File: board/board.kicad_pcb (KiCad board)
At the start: 2 copper layers, 43.2 x 53.3 mm, 73 parts, among them U2 10M02SCE144

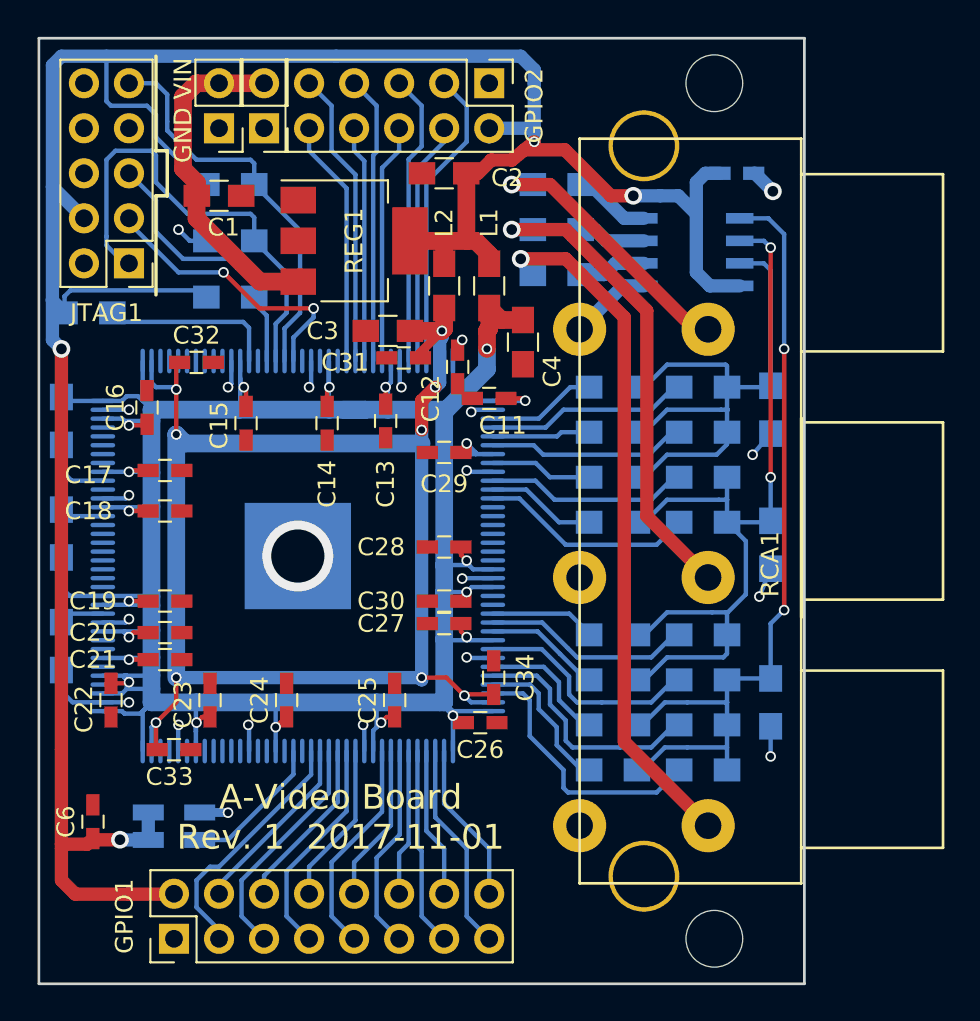
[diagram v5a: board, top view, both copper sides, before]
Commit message: Complete redo of the board
In Rev.1 I got GND and Line mixed up for the Video line sockets. As I
had to modify the board anyway, I also changed the location of the FPGA
from backside to front side and therefore had to redo everything.
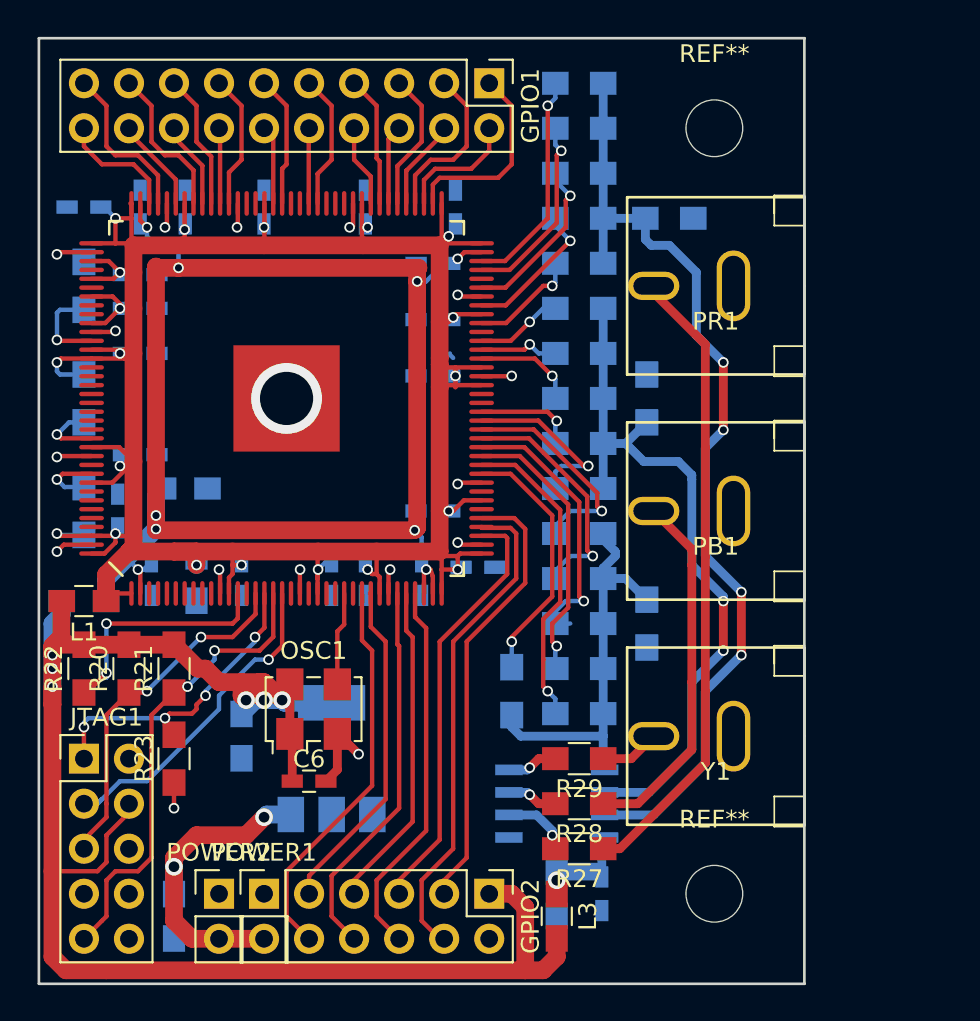
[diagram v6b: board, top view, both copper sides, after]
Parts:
- removed ? (x2): MountingHole_3.2mm_M3, Mounting_Holes:MountingHole_3.2mm_M3
- removed ?: CONN_02X01, Pin_Headers:Pin_Header_Straight_1x02_Pitch2.54mm
- removed C28, C29, C30: 100nF, Capacitors_SMD:C_0603_HandSoldering
- removed GND VIN: CONM_01x02, Pin_Headers:Pin_Header_Straight_1x02_Pitch2.54mm
- removed RCA1: TrippleRCA, footprints:TrippleRCA
- added C5: 10uF, Capacitors_SMD:C_0805_HandSoldering, B.Cu at (146.1, 119.4)
- added L3: 10mH, Capacitors_SMD:C_0805_HandSoldering, F.Cu at (146.1, 120.7)
- added PB1: BNC, footprints:RCA_JACK, F.Cu at (160.0, 97.8)
- added POWER1: CONM_01x02, Pin_Headers:Pin_Header_Straight_1x02_Pitch2.54mm, F.Cu at (129.5, 119.4)
- added POWER2: CONN_02X01, Pin_Headers:Pin_Header_Straight_1x02_Pitch2.54mm, F.Cu at (127.0, 119.4)
- added PR1: BNC, footprints:RCA_JACK, F.Cu at (160.0, 85.1)
- added REF**: MountingHole_3.2mm_M3, Mounting_Holes:MountingHole_3.2mm_M3, F.Cu at (154.9, 119.4)
- added REF**: MountingHole_3.2mm_M3, Mounting_Holes:MountingHole_3.2mm_M3, F.Cu at (154.9, 76.2)
- added Y1: BNC, footprints:RCA_JACK, F.Cu at (160.0, 110.5)
- C1, C11, C12, C13, C14, C15, C16, C17, C18, C19, C2, C20, C21, C22, C23, C24, C25, C26, C27, C3, C31, C32, C33, C34, C4, L2, REG1: moved to B.Cu
- GPIO1: value CONN_02X08 -> CONN_02X10; footprint Pin_Headers:Pin_Header_Straight_2x08_Pitch2.54mm -> Pin_Headers:Pin_Header_Straight_2x10_Pitch2.54mm
- OSC1: value XO32050UITA -> LFSPXO024957; footprint Oscillators:Oscillator_SMD_EuroQuartz_XO32-4pin_3.2x2.5mm_HandSoldering -> Oscillators:Oscillator_SMD_EuroQuartz_XO53-4pin_5.0x3.2mm_HandSoldering; moved to F.Cu
- R1: value 1k -> 1k1
- R10: value 10k -> 8k
- R11: value 10k -> 16k
- R14, R9: value 10k -> 4k
- R15: value 4k -> 8k
- R16: value 8k -> 16k
- R17: value 16k -> 150
- R19: value 1k -> 150
- R2: value 150 -> 1k
- R20: value 2k -> 10k; moved to F.Cu
- R21: value 4k -> 10k; moved to F.Cu
- R22: value 8k -> 10k; moved to F.Cu
- R23: value 16k -> 10k; moved to F.Cu
- R27, R28, R29, U2: moved to F.Cu
- R7: value 1k1 -> 1k
- R8: value 150 -> 2k
- moved GPIO1 51.4 mm to (142.2, 73.7), turned to 270 degrees
- moved GPIO2 45.7 mm to (142.2, 119.4)
- moved C7 41.3 mm to (148.6, 119.4), turned to 90 degrees
- moved C1 40.7 mm to (124.5, 120.7), turned to 270 degrees
- moved R27 37.5 mm to (147.3, 116.8), turned to 180 degrees
- moved C2 33.7 mm to (128.3, 110.5), turned to 270 degrees
- moved R28 32.4 mm to (147.3, 114.3), turned to 180 degrees
- moved AMP1 32.0 mm to (146.1, 114.3)
- moved R16 31.9 mm to (147.3, 73.7)
- moved R22 30.4 mm to (119.4, 106.7), turned to 90 degrees
- moved R21 30.0 mm to (124.5, 106.7), turned to 90 degrees
- moved R23 29.9 mm to (124.5, 111.8), turned to 90 degrees
- moved REG1 29.2 mm to (133.3, 111.8), turned to 90 degrees
- moved L1 29.0 mm to (119.4, 102.9), turned to 180 degrees
- moved R15 28.6 mm to (147.3, 76.2)
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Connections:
- AMP1 pad 4: /3V3A -> /3V3D
- C7 pad 2: /3V3A -> /3V3D
- GPIO1 pad 1: GND -> Net-(GPIO1-Pad1)
- GPIO1 pad 2: /3V3A -> Net-(GPIO1-Pad2)
- GPIO2 pad 1: GND -> /3V3A
- GPIO2 pad 2: /3V3A -> GND
- R1 pad 2: Net-(AMP1-Pad3) -> Net-(AMP1-Pad1)
- R10 pad 1: Net-(JTAG1-Pad9) -> Net-(R10-Pad1)
- R10 pad 2: /3V3A -> Net-(AMP1-Pad2)
- R11 pad 2: /3V3A -> Net-(AMP1-Pad2)
- R12 pad 2: Net-(AMP1-Pad2) -> Net-(AMP1-Pad3)
- R13 pad 2: Net-(AMP1-Pad2) -> Net-(AMP1-Pad3)
- R14 pad 1: GND -> Net-(R14-Pad1)
- R14 pad 2: Net-(JTAG1-Pad1) -> Net-(AMP1-Pad3)
- R15 pad 2: Net-(AMP1-Pad2) -> Net-(AMP1-Pad3)
- R16 pad 2: Net-(AMP1-Pad2) -> Net-(AMP1-Pad3)
- R17 pad 1: Net-(R17-Pad1) -> Net-(AMP1-Pad1)
- R17 pad 2: Net-(AMP1-Pad2) -> GND
- R18 pad 1: Net-(AMP1-Pad1) -> Net-(AMP1-Pad2)
- R19 pad 1: Net-(R19-Pad1) -> Net-(AMP1-Pad3)
- R19 pad 2: Net-(AMP1-Pad1) -> GND
- R2 pad 1: Net-(AMP1-Pad3) -> Net-(R2-Pad1)
- R2 pad 2: GND -> Net-(AMP1-Pad1)
- R20 pad 1: Net-(R20-Pad1) -> Net-(JTAG1-Pad5)
- R20 pad 2: Net-(AMP1-Pad1) -> /3V3A
- R21 pad 1: Net-(R21-Pad1) -> Net-(JTAG1-Pad9)
- R21 pad 2: Net-(AMP1-Pad1) -> /3V3A
- R22 pad 2: Net-(AMP1-Pad1) -> /3V3A
- R23 pad 1: Net-(R23-Pad1) -> GND
- R23 pad 2: Net-(AMP1-Pad1) -> Net-(JTAG1-Pad1)
- R27 pad 2: Net-(AMP1-Pad8) -> Net-(AMP1-Pad6)
- R29 pad 2: Net-(AMP1-Pad6) -> Net-(AMP1-Pad8)
- R3 pad 2: Net-(AMP1-Pad3) -> Net-(AMP1-Pad1)
- R4 pad 2: Net-(AMP1-Pad3) -> Net-(AMP1-Pad1)
- R5 pad 2: Net-(AMP1-Pad3) -> Net-(AMP1-Pad1)
- R6 pad 2: Net-(AMP1-Pad3) -> Net-(AMP1-Pad1)
- R8 pad 1: Net-(AMP1-Pad2) -> Net-(R8-Pad1)
- R8 pad 2: GND -> Net-(AMP1-Pad2)
- R9 pad 1: Net-(JTAG1-Pad5) -> Net-(R9-Pad1)
- R9 pad 2: /3V3A -> Net-(AMP1-Pad2)
- U2 pad 100: (no net) -> Net-(GPIO1-Pad16)
- U2 pad 101: (no net) -> Net-(GPIO1-Pad17)
- U2 pad 103: (no net) -> Net-(GPIO1-Pad18)
- U2 pad 105: (no net) -> Net-(GPIO1-Pad19)
- U2 pad 106: (no net) -> Net-(GPIO1-Pad20)
- U2 pad 13: Net-(R11-Pad1) -> Net-(R22-Pad1)
- U2 pad 24: Net-(GPIO2-Pad10) -> (no net)
- U2 pad 25: Net-(GPIO2-Pad9) -> Net-(OSC1-Pad3)
- U2 pad 26: Net-(GPIO2-Pad8) -> (no net)
- U2 pad 27: Net-(GPIO2-Pad7) -> Net-(GPIO2-Pad10)
- U2 pad 28: Net-(GPIO2-Pad6) -> Net-(GPIO2-Pad9)
- U2 pad 31: Net-(GPIO2-Pad5) -> Net-(GPIO2-Pad8)
- U2 pad 32: Net-(GPIO2-Pad4) -> Net-(GPIO2-Pad7)
- U2 pad 33: Net-(GPIO2-Pad3) -> Net-(GPIO2-Pad6)
- U2 pad 39: Net-(R1-Pad1) -> Net-(GPIO2-Pad5)
- U2 pad 40: Net-(R3-Pad1) -> Net-(GPIO2-Pad4)
- U2 pad 41: Net-(R4-Pad1) -> Net-(GPIO2-Pad3)
- U2 pad 42: Net-(R5-Pad1) -> (no net)
- U2 pad 44: Net-(R6-Pad1) -> (no net)
- U2 pad 46: Net-(R7-Pad1) -> Net-(R1-Pad1)
- U2 pad 47: Net-(R12-Pad1) -> Net-(R2-Pad1)
- U2 pad 48: Net-(R13-Pad1) -> Net-(R3-Pad1)
- U2 pad 49: (no net) -> Net-(R4-Pad1)
- U2 pad 50: (no net) -> Net-(R5-Pad1)
- U2 pad 51: (no net) -> Net-(R6-Pad1)
- U2 pad 52: (no net) -> Net-(R7-Pad1)
- U2 pad 53: (no net) -> Net-(R8-Pad1)
- U2 pad 59: (no net) -> Net-(R9-Pad1)
- U2 pad 60: (no net) -> Net-(R10-Pad1)
- U2 pad 61: Net-(R15-Pad1) -> Net-(R11-Pad1)
- U2 pad 62: Net-(R16-Pad1) -> (no net)
- U2 pad 63: Net-(R17-Pad1) -> Net-(R12-Pad1)
- U2 pad 65: Net-(R19-Pad1) -> Net-(R13-Pad1)
- U2 pad 67: Net-(R20-Pad1) -> Net-(R14-Pad1)
- U2 pad 68: Net-(R21-Pad1) -> (no net)
- U2 pad 69: Net-(R22-Pad1) -> Net-(R15-Pad1)
- U2 pad 70: Net-(R23-Pad1) -> Net-(R16-Pad1)
- U2 pad 74: Net-(GPIO1-Pad16) -> Net-(GPIO1-Pad1)
- U2 pad 75: Net-(GPIO1-Pad15) -> Net-(GPIO1-Pad2)
- U2 pad 76: Net-(GPIO1-Pad14) -> Net-(GPIO1-Pad3)
- U2 pad 77: Net-(GPIO1-Pad13) -> Net-(GPIO1-Pad4)
- U2 pad 78: Net-(GPIO1-Pad12) -> Net-(GPIO1-Pad5)
- U2 pad 79: Net-(GPIO1-Pad11) -> Net-(GPIO1-Pad6)
- U2 pad 80: Net-(GPIO1-Pad10) -> Net-(GPIO1-Pad7)
- U2 pad 81: Net-(GPIO1-Pad9) -> Net-(GPIO1-Pad8)
- U2 pad 84: Net-(GPIO1-Pad8) -> (no net)
- U2 pad 85: Net-(GPIO1-Pad7) -> (no net)
- U2 pad 86: Net-(GPIO1-Pad6) -> (no net)
- U2 pad 87: Net-(GPIO1-Pad5) -> Net-(GPIO1-Pad9)
- U2 pad 88: Net-(GPIO1-Pad4) -> Net-(GPIO1-Pad10)
- U2 pad 89: Net-(GPIO1-Pad3) -> (no net)
- U2 pad 91: Net-(OSC1-Pad3) -> Net-(GPIO1-Pad11)
- U2 pad 92: (no net) -> Net-(GPIO1-Pad12)
- U2 pad 97: (no net) -> Net-(GPIO1-Pad13)
- U2 pad 98: (no net) -> Net-(GPIO1-Pad14)
- U2 pad 99: (no net) -> Net-(GPIO1-Pad15)
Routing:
- net /3V3A: track 153.7 -> 99.8 mm, vias 4 -> 6
- net Net-(R29-Pad1): track 39.0 -> 3.38 mm, vias 1 -> 0
- net /3V3B: track 190.5 -> 166.0 mm, vias 21 -> 20
- net Net-(AMP1-Pad1): track 47.3 -> 23.2 mm, vias 2 -> 0
- net Net-(AMP1-Pad3): track 32.5 -> 54.7 mm, vias 0 -> 4
- net Net-(PR1-Pad1): track 16.9 -> 35.9 mm, vias 1 -> 0
- net Net-(R2-Pad1): track 0.00 -> 17.8 mm, vias 0 -> 1
- net Net-(R23-Pad1): track 15.1 -> 0.00 mm
- net Net-(R21-Pad1): track 13.9 -> 0.00 mm
- net Net-(GPIO2-Pad4): track 14.3 -> 27.9 mm
- net Net-(R19-Pad1): track 12.9 -> 0.00 mm
- net GND: track 39.5 -> 27.8 mm, vias 21 -> 17
- net Net-(GPIO1-Pad1): track 0.00 -> 11.1 mm
- net Net-(R4-Pad1): track 5.53 -> 15.9 mm, vias 0 -> 1
- net Net-(R14-Pad1): track 0.00 -> 9.66 mm, vias 0 -> 1
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- added copper zone on B.Cu, net GND
- removed copper zone on F.Cu, net GND
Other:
- board text removed: "A-Video Board Rev. 1 2017-11-01"

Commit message: finalize board layout
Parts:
- added REF***: OSHW-Logo2_7.3x6mm_SilkScreen, Symbols:OSHW-Logo2_7.3x6mm_SilkScreen, F.Cu at (139.2, 110.5)
- renumbered REF** to ?, POWER1 to GND, POWER2 to GND
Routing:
- net Net-(AMP1-Pad2): track 40.5 -> 38.7 mm
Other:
- outline, holes or cut-outs redrawn
- board text added: "1"
- board text added: "A-Video Board Rev. 2 github.com/c0pperdragon"
- board text added: "VIN"

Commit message: created gerber files
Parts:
- removed ? (x2): MountingHole_3.2mm_M3, Mounting_Holes:MountingHole_3.2mm_M3
- added REF**: MountingHole_3.2mm_M3_DIN965_Pad, Mounting_Holes:MountingHole_3.2mm_M3_DIN965_Pad, F.Cu at (154.9, 76.2)
- added REF**: MountingHole_3.2mm_M3_DIN965_Pad, Mounting_Holes:MountingHole_3.2mm_M3_DIN965_Pad, F.Cu at (154.9, 119.4)
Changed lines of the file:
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@@
     (links 214)
     (no_connects 0)
-    (area 116.764999 71.044999 160.095001 124.535001)
+    (area 115.616667 69.896666 164.497143 125.683333)
     (thickness 1.6)
     (drawings 51)
@@
   )
   (setup
-    (last_trace_width 0.5)
+    (last_trace_width 0.25)
     (user_trace_width 0.4)
     (user_trace_width 0.5)
@@
     )
   )
-  (module Mounting_Holes:MountingHole_3.2mm_M3 (layer F.Cu)
-    (at 154.94 119.38)
-    (descr "Mounting Hole 3.2mm, no annular, M3")
-    (tags "mounting hole 3.2mm no annular m3")
-    (attr virtual)
-    (fp_text reference "" (at 0 -4.2) (layer F.SilkS)
-      (effects (font (size 1 1) (thickness 0.15)))
-    )
-    (fp_text value MountingHole_3.2mm_M3 (at 0 4.2) (layer F.Fab)
-      (effects (font (size 1 1) (thickness 0.15)))
-    )
-    (fp_text user %R (at 0.3 0) (layer F.Fab)
-      (effects (font (size 1 1) (thickness 0.15)))
-    )
-    (fp_circle (center 0 0) (end 3.2 0) (layer Cmts.User) (width 0.15))
-    (fp_circle (center 0 0) (end 3.45 0) (layer F.CrtYd) (width 0.05))
-    (pad 1 np_thru_hole circle (at 0 0) (size 3.2 3.2) (drill 3.2) (layers *.Cu *.Mask))
-  )
-  (module Mounting_Holes:MountingHole_3.2mm_M3 (layer F.Cu)
-    (at 154.94 76.2)
-    (descr "Mounting Hole 3.2mm, no annular, M3")
-    (tags "mounting hole 3.2mm no annular m3")
-    (attr virtual)
-    (fp_text reference "" (at 0 -4.2) (layer F.SilkS)
-      (effects (font (size 1 1) (thickness 0.15)))
-    )
-    (fp_text value MountingHole_3.2mm_M3 (at 0 4.2) (layer F.Fab)
-      (effects (font (size 1 1) (thickness 0.15)))
-    )
-    (fp_text user %R (at 0.3 0) (layer F.Fab)
-      (effects (font (size 1 1) (thickness 0.15)))
-    )
-    (fp_circle (center 0 0) (end 3.2 0) (layer Cmts.User) (width 0.15))
-    (fp_circle (center 0 0) (end 3.45 0) (layer F.CrtYd) (width 0.05))
-    (pad 1 np_thru_hole circle (at 0 0) (size 3.2 3.2) (drill 3.2) (layers *.Cu *.Mask))
-  )
   (module Symbols:OSHW-Logo2_7.3x6mm_SilkScreen (layer F.Cu)
     (at 139.192 110.49 90)
@@
       (xy -0.113933 -2.757629) (xy -0.013056 -2.757714) (xy 0 -2.757714) (xy 0.10391 -2.757652)) (layer F.SilkS) (width 0.01))
   )
+  (module Mounting_Holes:MountingHole_3.2mm_M3_DIN965_Pad (layer F.Cu)
+    (at 154.94 76.2)
+    (descr "Mounting Hole 3.2mm, M3, DIN965")
+    (tags "mounting hole 3.2mm m3 din965")
+    (attr virtual)
+    (fp_text reference REF** (at 0 -3.8) (layer F.SilkS)
+      (effects (font (size 1 1) (thickness 0.15)))
+    )
+    (fp_text value MountingHole_3.2mm_M3_DIN965_Pad (at 0 3.8) (layer F.Fab)
+      (effects (font (size 1 1) (thickness 0.15)))
+    )
+    (fp_text user %R (at 0.3 0) (layer F.Fab)
+      (effects (font (size 1 1) (thickness 0.15)))
+    )
+    (fp_circle (center 0 0) (end 2.8 0) (layer Cmts.User) (width 0.15))
+    (fp_circle (center 0 0) (end 3.05 0) (layer F.CrtYd) (width 0.05))
+    (pad 1 thru_hole circle (at 0 0) (size 5.6 5.6) (drill 3.2) (layers *.Cu *.Mask))
+  )
+  (module Mounting_Holes:MountingHole_3.2mm_M3_DIN965_Pad (layer F.Cu)
+    (at 154.94 119.38)
+    (descr "Mounting Hole 3.2mm, M3, DIN965")
+    (tags "mounting hole 3.2mm m3 din965")
+    (attr virtual)
+    (fp_text reference REF** (at 0 -3.8) (layer F.SilkS)
+      (effects (font (size 1 1) (thickness 0.15)))
+    )
+    (fp_text value MountingHole_3.2mm_M3_DIN965_Pad (at 0 3.8) (layer F.Fab)
+      (effects (font (size 1 1) (thickness 0.15)))
+    )
+    (fp_text user %R (at 0.3 0) (layer F.Fab)
+      (effects (font (size 1 1) (thickness 0.15)))
+    )
+    (fp_circle (center 0 0) (end 2.8 0) (layer Cmts.User) (width 0.15))
+    (fp_circle (center 0 0) (end 3.05 0) (layer F.CrtYd) (width 0.05))
+    (pad 1 thru_hole circle (at 0 0) (size 5.6 5.6) (drill 3.2) (layers *.Cu *.Mask))
+  )
   (gr_line (start 117.856 115.316) (end 117.856 110.49) (angle 90) (layer F.SilkS) (width 0.2))
